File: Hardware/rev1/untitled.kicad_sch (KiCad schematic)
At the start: 17 parts, among them J3 Screw_Terminal_01x02, U2 HT75xx-1-SOT89

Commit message: UUUUHHH
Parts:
- removed C1: 4.7u, symbol Device:C
- removed C2, C3, C4, C5: 100n, symbol Device:C
- added BZ1: Buzzer, symbol Device:Buzzer
- added C10: 1u, symbol Device:C
- added SW1: SW_Push, symbol Switch:SW_Push
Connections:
- net GND: now also BZ1.2 (-), C10.2, SW1.2
- new net Buzzer_Channel: BZ1.1 (+)
- new net System_Reset: C10.1, SW1.1

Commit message: h
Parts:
- removed BZ1: Buzzer, symbol Device:Buzzer
- removed C6: 10n, symbol Device:C
- removed D1: D, symbol Device:D
- removed D3: LED, symbol Device:LED
- removed SW1: SW_Push, symbol Switch:SW_Push
- added D1: LED, symbol Device:LED
- added D3: D, symbol Device:D
- added J2: USB_C_Receptacle_USB2.0_14P, symbol Connector:USB_C_Receptacle_USB2.0_14P
- added R1: 1k5, Resistor_SMD:R_0402_1005Metric, symbol Device:R
- added R2: 0, symbol Device:R
- added R4: 5k1, Resistor_SMD:R_0402_1005Metric, symbol Device:R
- C10: value 1u -> 10u
- C7: value 1u -> 10n
- C8: value 10u -> 1u
- R3: value 0 -> 1k5; footprint (none) -> Resistor_SMD:R_0402_1005Metric; now fitted
- R5: value 1k5 -> 5k1
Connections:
- net System_Reset is gone; now on net +3V3: C10.1
- net +3.3V: now also R3.2, D1.2 (A), R2.1; no longer R3.1
- net +3.3VA: now also C8.1, R2.2; no longer R3.2
- net +3V3: no longer C9.1
- net +BATT: now also D2.2 (A)
- net GND: now also J2.A1 (GND), J2.A12 (GND), J2.B1 (GND), J2.B12 (GND), J2.S1 (SHIELD), R1.2, R4.1
- net VBUS: now also D3.2 (A), J2.A4 (VBUS), J2.A9 (VBUS), J2.B4 (VBUS), J2.B9 (VBUS); no longer D2.2 (A)
- net at R5.1: now also J2.B5 (CC2)
- net at J3.2 (Pin_2), U2.2 (VIN): now also C9.1; no longer C8.1
- net at D2.1 (K), J3.1 (Pin_1): now also D3.1 (K)
- new net: D1.1 (K), R1.1
- new net: J2.A5 (CC1), R4.2
- new net D+: J2.A6 (D+), J2.B6 (D+), R3.1
- new net D-: J2.A7 (D-), J2.B7 (D-)

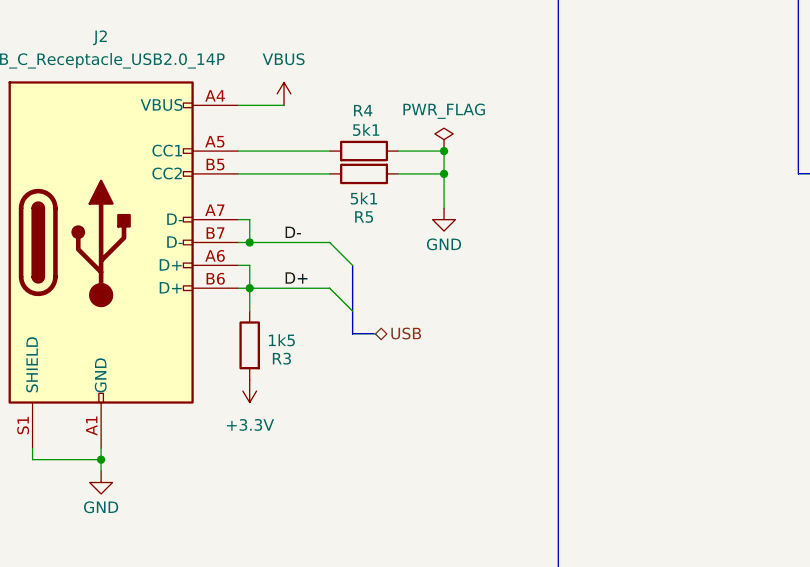
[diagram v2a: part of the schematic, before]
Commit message: Fixed the Errors
The Nets i tells ya, the nets!
need to specify the signals in the hierarchal labels
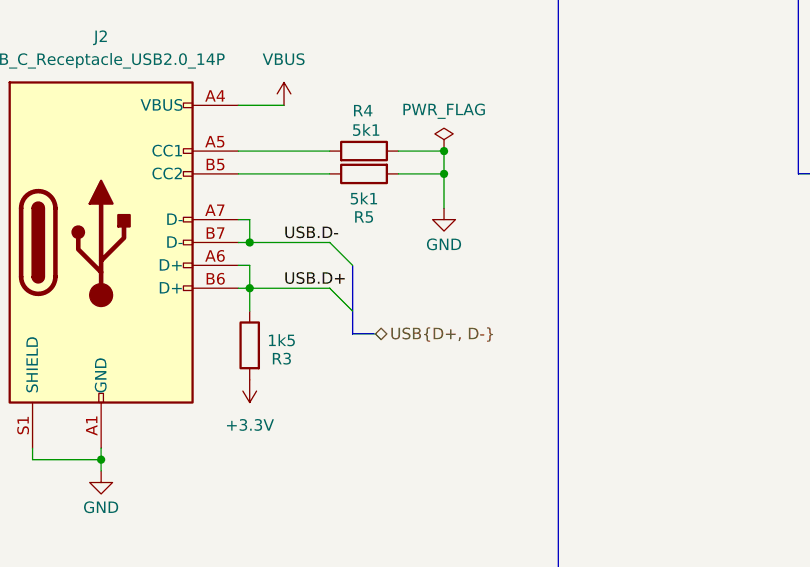
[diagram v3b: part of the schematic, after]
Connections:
- net D+ renamed USB.D+
- net D- renamed USB.D-
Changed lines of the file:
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@@
 		)
 	)
-	(label "D+"
+	(label "USB.D+"
 		(at 72.39 66.04 0)
 		(fields_autoplaced yes)
@@
 		)
 	)
-	(label "D-"
+	(label "USB.D-"
 		(at 72.39 60.96 0)
 		(fields_autoplaced yes)
@@
 		)
 	)
-	(hierarchical_label "USB"
+	(hierarchical_label "USB{D+, D-}"
 		(shape bidirectional)
 		(at 82.55 71.12 0)
@@
 			(justify left)
 		)
+		(property "USB.D-" ""
+			(at 82.55 72.39 0)
+			(effects
+				(font
+					(size 1.27 1.27)
+					(italic yes)
+				)
+				(justify left)
+			)
+		)
+		(property "USB.D+" ""
+			(at 82.55 74.041 0)
+			(effects
+				(font
+					(size 1.27 1.27)
+					(italic yes)
+				)
+				(justify left)
+			)
+		)
 	)

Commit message: Add buses (maybe)
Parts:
- removed R2: 0, symbol Device:R
- added NT1: NetTie_2, symbol Device:NetTie_2
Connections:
- net +3.3V: now also NT1.1
- net +3.3VA: now also NT1.2
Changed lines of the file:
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@@
 	(wire
 		(pts
-			(xy 226.06 92.71) (xy 229.87 92.71)
+			(xy 224.79 92.71) (xy 229.87 92.71)
 		)
 		(stroke
@@
 	(wire
 		(pts
-			(xy 214.63 92.71) (xy 218.44 92.71)
+			(xy 214.63 92.71) (xy 219.71 92.71)
 		)
 		(stroke
@@
 	)
 	(symbol
-		(lib_id "Device:R")
-		(at 222.25 92.71 90)
-		(unit 1)
-		(exclude_from_sim no)
-		(in_bom yes)
-		(on_board yes)
-		(dnp yes)
-		(fields_autoplaced yes)
-		(property "Reference" "R2"
-			(at 222.25 86.36 90)
-			(effects
-				(font
-					(size 1.27 1.27)
-				)
-			)
-		)
-		(property "Value" "0"
-			(at 222.25 88.9 90)
-			(effects
-				(font
-					(size 1.27 1.27)
-				)
-			)
-		)
-		(property "Footprint" ""
-			(at 222.25 94.488 90)
-			(effects
-				(font
-					(size 1.27 1.27)
-				)
-				(hide yes)
-			)
-		)
-		(property "Datasheet" "~"
-			(at 222.25 92.71 0)
-			(effects
-				(font
-					(size 1.27 1.27)
-				)
-				(hide yes)
-			)
-		)
-		(property "Description" "Resistor"
-			(at 222.25 92.71 0)
-			(effects
-				(font
-					(size 1.27 1.27)
-				)
-				(hide yes)
-			)
-		)
-		(pin "2"
-		)
-		(pin "1"
-		)
-		(instances
-			(project "rev1"
-				(path "/e52639ab-1647-4d34-8bc5-5aadc4708147/28e3f1a4-a9ec-420d-b6dc-1cdf5f0e43fa"
-					(reference "R2")
-					(unit 1)
-				)
-			)
-		)
-	)
-	(symbol
 		(lib_id "power:+BATT")
 		(at 153.67 146.05 0)
@@
 					(unit 1)
 				)
+			)
+		)
+	)
+	(symbol
+		(lib_id "Device:NetTie_2")
+		(at 222.25 92.71 0)
+		(unit 1)
+		(exclude_from_sim no)
+		(in_bom no)
+		(on_board yes)
+		(dnp no)
+		(fields_autoplaced yes)
+		(property "Reference" "NT1"
+			(at 222.25 87.63 0)
+			(effects
+				(font
+					(size 1.27 1.27)
+				)
+			)
+		)
+		(property "Value" "NetTie_2"
+			(at 222.25 90.17 0)
+			(effects
+				(font
+					(size 1.27 1.27)
+				)
+			)
+		)
+		(property "Footprint" ""
+			(at 222.25 92.71 0)
+			(effects
+				(font
+					(size 1.27 1.27)
+				)
+				(hide yes)
+			)
+		)
+		(property "Datasheet" "~"
+			(at 222.25 92.71 0)
+			(effects
+				(font
+					(size 1.27 1.27)
+				)
+				(hide yes)
+			)
+		)
+		(property "Description" "Net tie, 2 pins"
+			(at 222.25 92.71 0)
+			(effects
+				(font
+					(size 1.27 1.27)
+				)
+				(hide yes)
+			)
+		)
+		(pin "1"
+		)
+		(pin "2"
+		)
+		(instances
+			(project ""
+				(path "/e52639ab-1647-4d34-8bc5-5aadc4708147/28e3f1a4-a9ec-420d-b6dc-1cdf5f0e43fa"
+					(reference "NT1")
+					(unit 1)
+				)

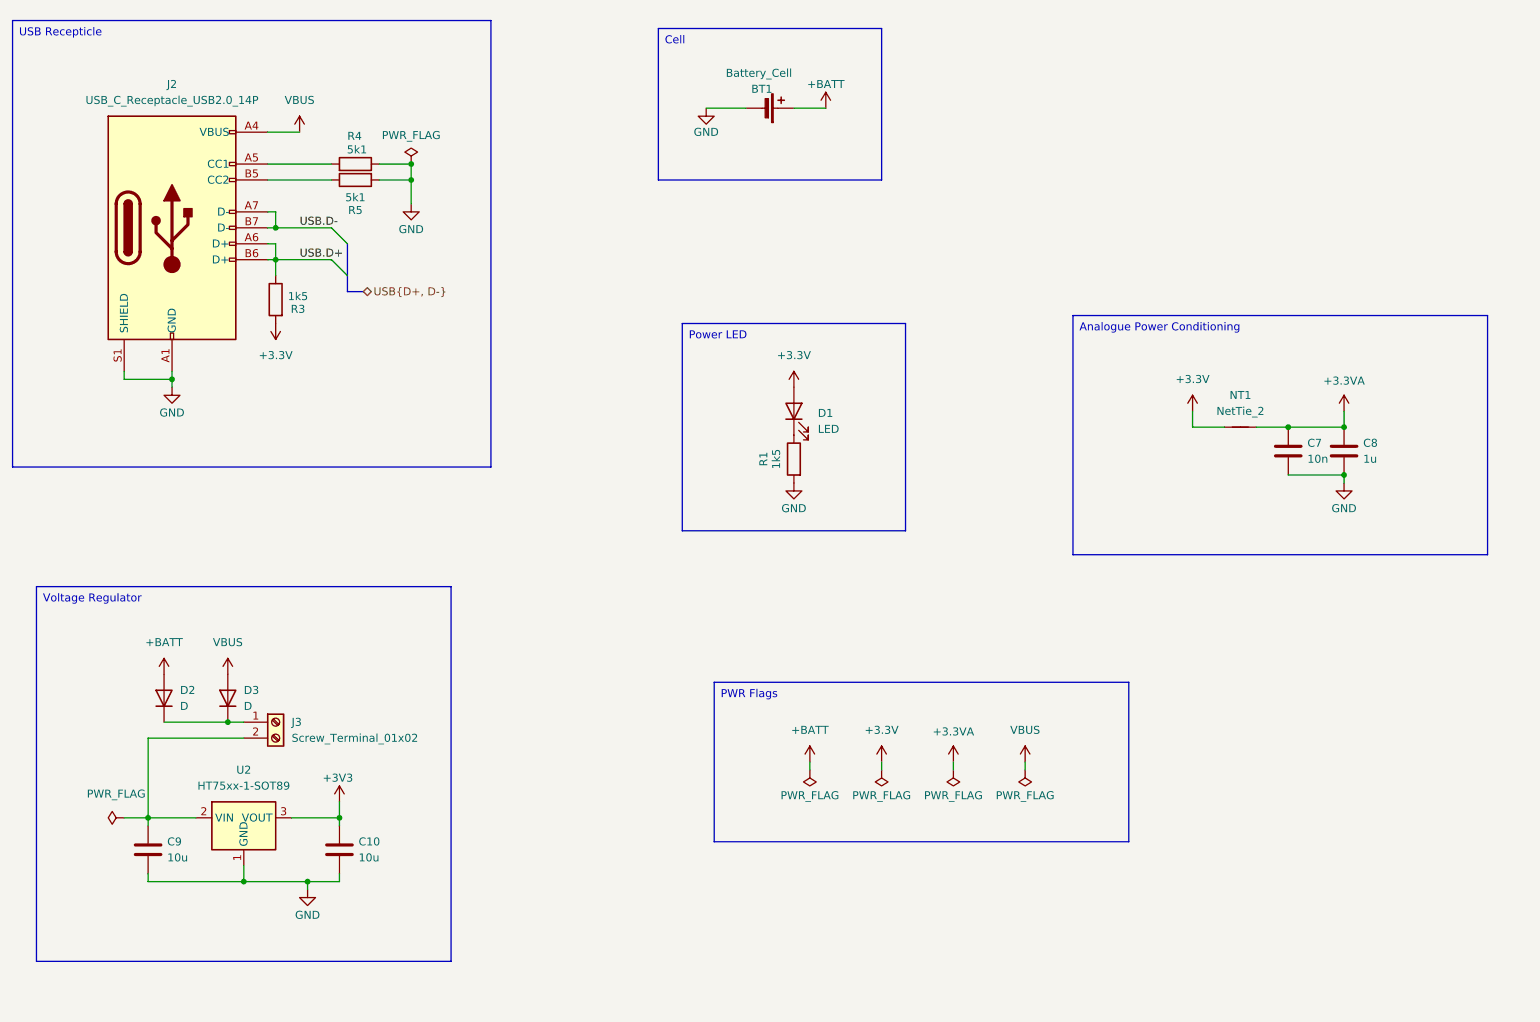
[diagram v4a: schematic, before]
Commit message: GitHub Shenanegans - Taken things from Shon's commit because easier to fix that way than to figure out how to merge properly
Literally for the buzzer and switch, hopefully retain the capacitor fix
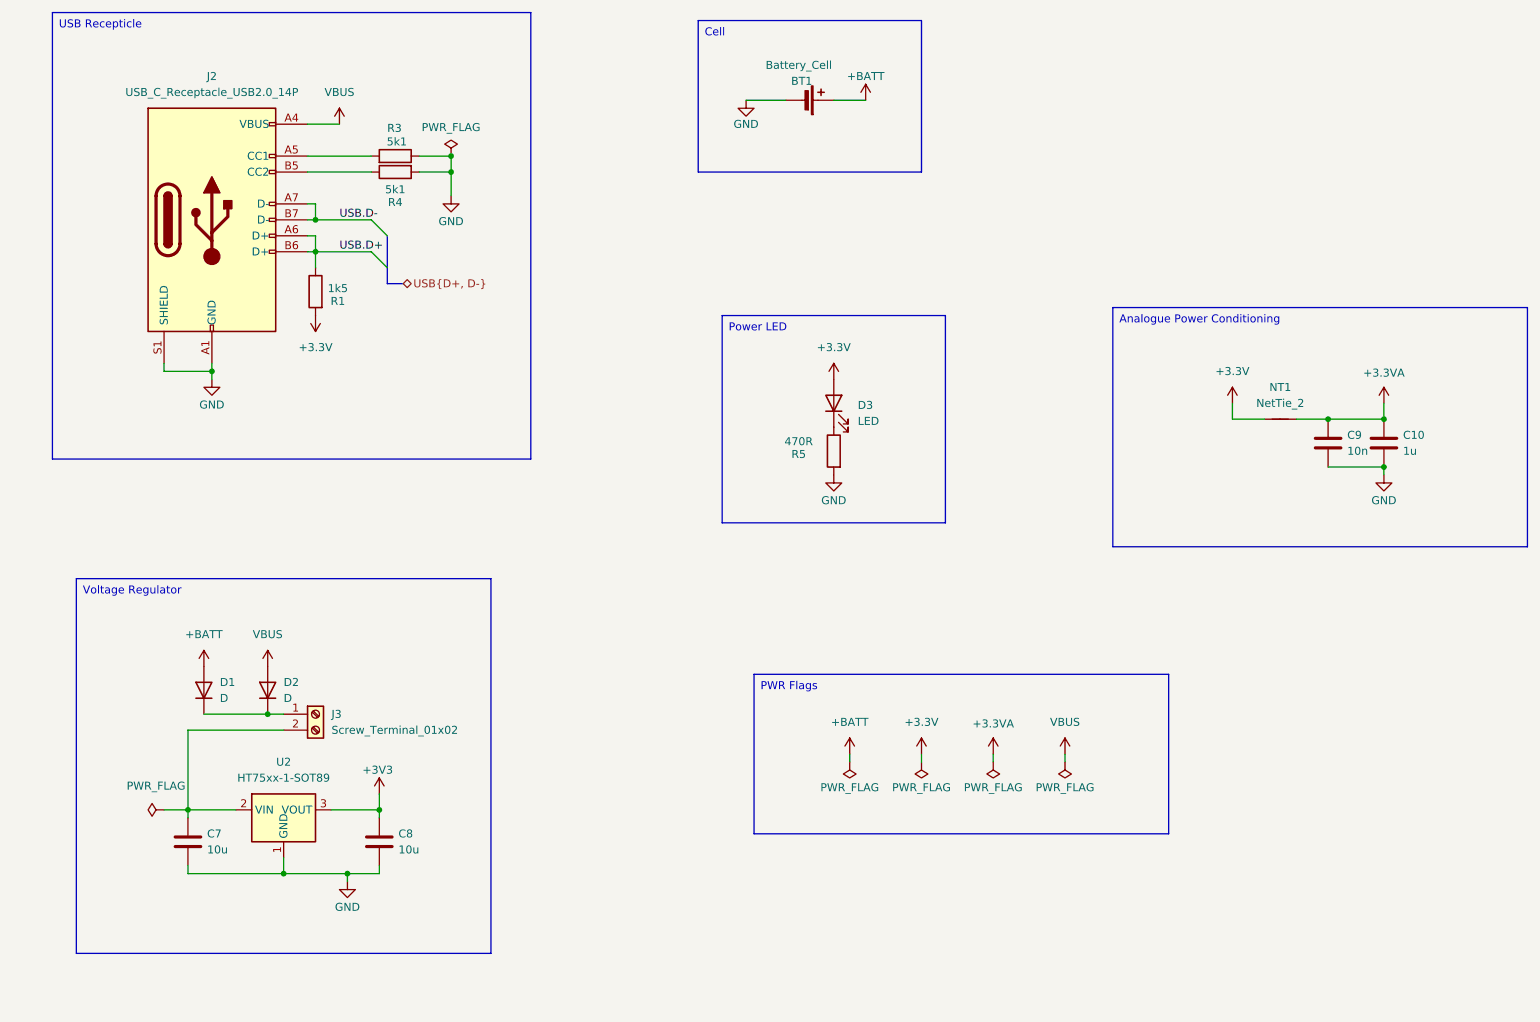
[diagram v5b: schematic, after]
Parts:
- removed D1: LED, symbol Device:LED
- removed D3: D, symbol Device:D
- added D1: D, Diode_SMD:D_SOD-123F, symbol Device:D
- added D3: LED, LED_SMD:LED_0201_0603Metric, symbol Device:LED
- BT1: footprint (none) -> Battery:BatteryHolder_Keystone_3034_1x20mm
- C10: value 10u -> 1u; footprint (none) -> Capacitor_SMD:C_0603_1608Metric
- C7: value 10n -> 10u; footprint (none) -> Capacitor_SMD:C_0603_1608Metric
- C8: value 1u -> 10u; footprint (none) -> Capacitor_SMD:C_0603_1608Metric
- C9: value 10u -> 10n; footprint (none) -> Capacitor_SMD:C_0402_1005Metric
- D2: footprint (none) -> Diode_SMD:D_SOD-123F
- J2: footprint (none) -> Connector_USB:USB_C_Receptacle_HRO_TYPE-C-31-M-12
- J3: footprint (none) -> TerminalBlock:TerminalBlock_Xinya_XY308-2.54-2P_1x02_P2.54mm_Horizontal
- NT1: footprint (none) -> NetTie:NetTie-2_SMD_Pad2.0mm
- R1, R4: footprint Resistor_SMD:R_0402_1005Metric -> Resistor_SMD:R_0603_1608Metric
- R3: value 1k5 -> 5k1; footprint Resistor_SMD:R_0402_1005Metric -> Resistor_SMD:R_0603_1608Metric
- R5: value 5k1 -> 470R; footprint Resistor_SMD:R_0402_1005Metric -> Resistor_SMD:R_0603_1608Metric
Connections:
- net +3.3V: now also R1.2, D3.2 (A); no longer R3.2
- net +3.3VA: now also C10.1, C9.1; no longer C7.1, C8.1
- net +3V3: now also C8.1; no longer C10.1
- net +BATT: now also D1.2 (A); no longer D2.2 (A)
- net GND: now also R3.1, R4.2; no longer R1.2, R4.1
- net USB.D+: now also R1.1; no longer R3.1
- net VBUS: now also D2.2 (A)
- net at J3.2 (Pin_2), U2.2 (VIN): now also C7.1; no longer C9.1
- net at D2.1 (K), J3.1 (Pin_1): now also D1.1 (K)
- net at J2.A5 (CC1): now also R3.2; no longer R4.2
- net at J2.B5 (CC2): now also R4.1; no longer R5.1
- new net: D3.1 (K), R5.1
